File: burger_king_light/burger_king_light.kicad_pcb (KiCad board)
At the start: 2 copper layers, 102.1 x 58.7 mm, 57 parts, among them U1 TPS55340PWPR, U2 ICM7555CBAZ, U3 IS32LT3178-GRLA3-TR, U4 IS32LT3178-GRLA3-TR, U5 IS32LT3178-GRLA3-TR

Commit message: resized pot footprint, redid routing for 555 circuit. added ground planes to F.Cu with via stitching
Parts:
- H1, H2, H3, H4, H5, H6, H7, H8: footprint MountingHole:MountingHole_3.5mm_Pad_TopBottom -> MountingHole:MountingHole_2.5mm_Pad_TopBottom
- moved RV1 13.0 mm to (86.2, 124.5)
- moved D4 9.62 mm to (93.2, 116.6), turned to 90 degrees
- moved D3 8.92 mm to (99.3, 116.6), turned to -90 degrees
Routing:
- net Net-(D4-K): track 11.5 -> 4.31 mm
- net PWM out: track 134.5 -> 138.7 mm
- net Net-(R3-Pad2): track 23.6 -> 19.4 mm
- net Net-(D3-A): track 6.98 -> 4.46 mm
- net 0: vias 152 -> 169

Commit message: added logo and fixed silkscreens. passes DRC, ready for assembly, v1.0
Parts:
- added G***: LOGO, custom_logos:spectrum-designs, F.Cu at (75.6, 74.5)
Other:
- board text added: "BK LED Control v1.0"

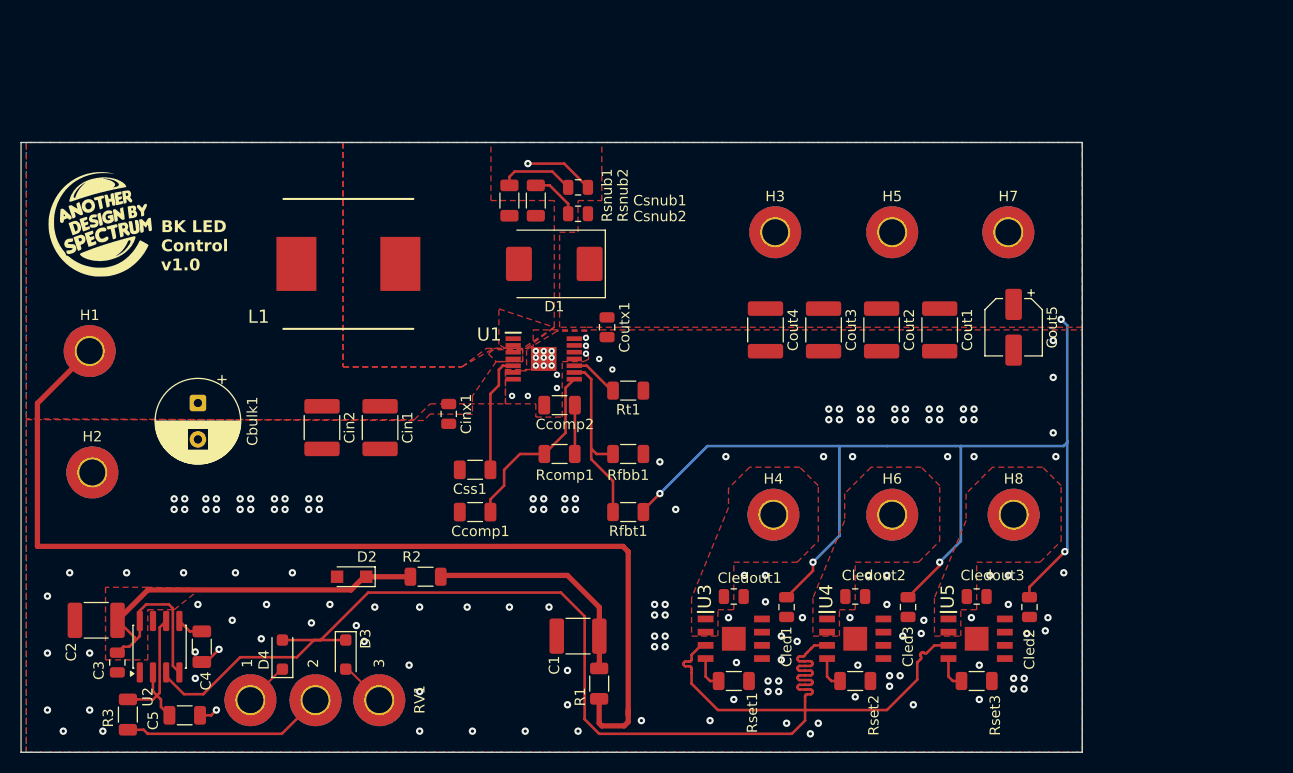
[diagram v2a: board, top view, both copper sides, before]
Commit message: reduced size of board, rerouted connections for LED controllers. rounded tracks. passed DRC, ready for fab, v1.1
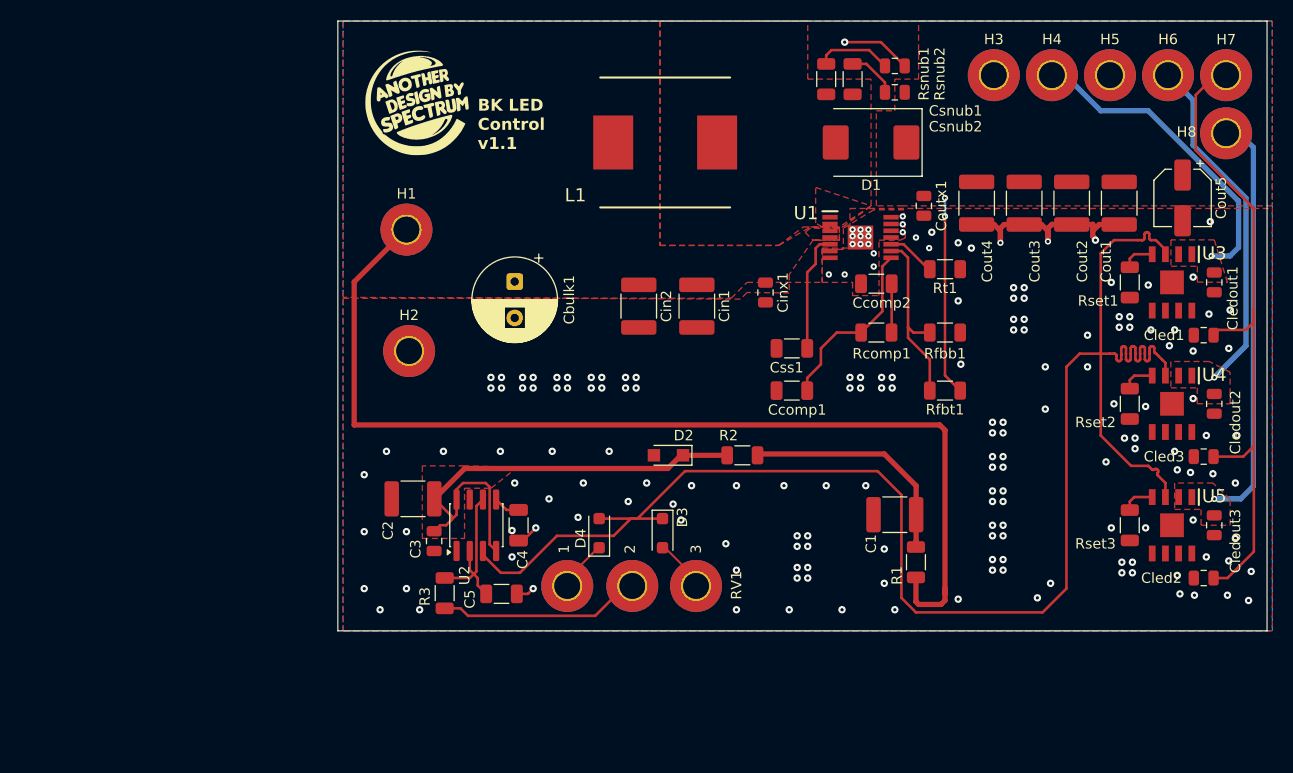
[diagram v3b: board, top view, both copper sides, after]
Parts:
- moved Cledout1 55.2 mm to (182.9, 80.8), turned to -90 degrees
- moved U3 54.3 mm to (178.8, 80.8), turned to -90 degrees
- moved Rset1 54.1 mm to (174.8, 80.8), turned to -90 degrees
- moved H4 50.1 mm to (167.3, 60.8)
- moved H6 49.9 mm to (178.4, 60.8)
- moved Cled1 47.9 mm to (181.9, 85.9), turned to 180 degrees
- moved H8 42.0 mm to (184.0, 66.4)
- moved Cledout2 39.2 mm to (182.9, 92.5), turned to -90 degrees
- moved U4 37.9 mm to (178.8, 92.5), turned to -90 degrees
- moved Rset2 37.5 mm to (174.8, 92.5), turned to -90 degrees
- moved D1 32.6 mm to (149.9, 67.3)
- moved D3 32.6 mm to (129.8, 104.9)
- moved H1 32.6 mm to (105.2, 75.7)
- moved Rt1 32.6 mm to (157.0, 79.5)
- moved C5 32.6 mm to (114.3, 110.7)
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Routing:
- net Net-(U5-OUT_1): track 0.00 -> 40.4 mm, vias 0 -> 1
- net Net-(U4-OUT_1): track 0.00 -> 33.4 mm, vias 0 -> 1
- net Net-(U3-OUT_1): track 0.00 -> 31.2 mm, vias 0 -> 1
- net 0: track 10.7 -> 31.9 mm, vias 169 -> 180
- net +36V: track 105.6 -> 84.8 mm, vias 5 -> 2
- net PWM out: track 138.7 -> 158.7 mm
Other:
- board size 102.1 x 58.7 mm -> 89.4 x 58.7 mm
- board text added: "BK LED Control v1.1"
- board text removed: "BK LED Control v1.0"
